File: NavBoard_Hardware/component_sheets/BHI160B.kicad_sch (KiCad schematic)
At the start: 12 parts, among them U2 BHI160B

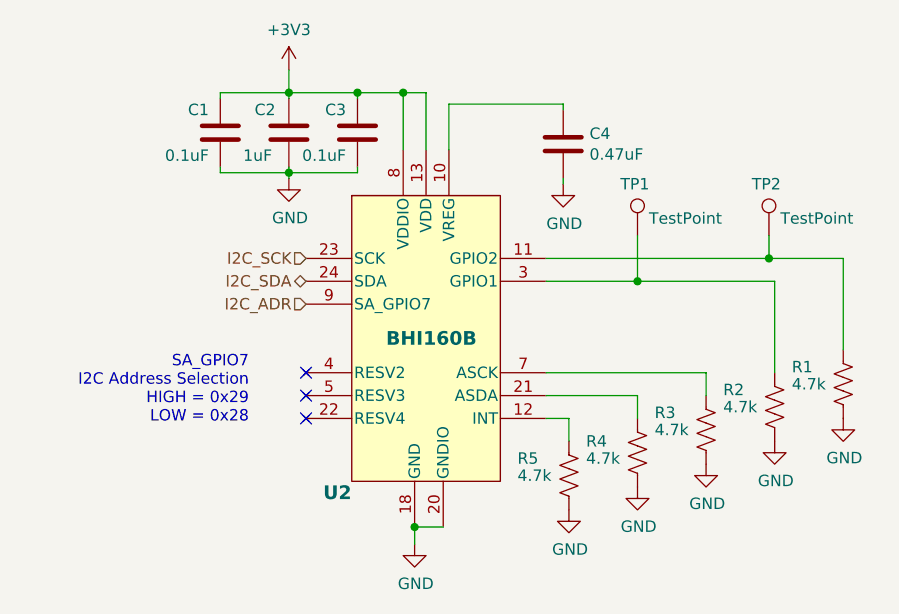
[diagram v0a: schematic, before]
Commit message: Most connections made on schematic
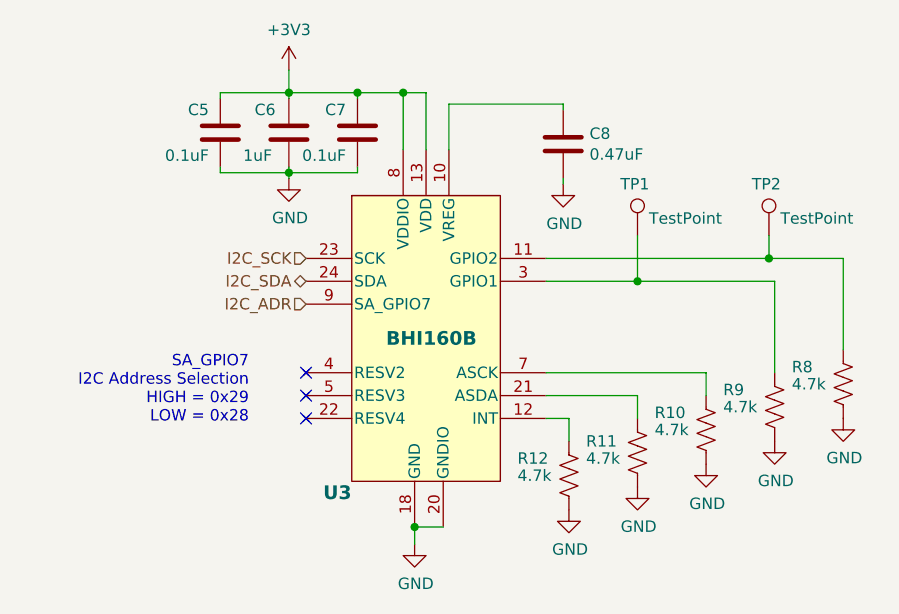
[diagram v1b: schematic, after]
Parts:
- renumbered C1 to C5, C2 to C6, C3 to C7, C4 to C8, R3 to R10, R4 to R11, R5 to R12, R1 to R8, R2 to R9, U2 to U3
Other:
- title: MRDT NavBoard - BHI160B -> MRDT NavBoard
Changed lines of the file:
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@@
   (paper "A4")
   (title_block
-    (title "MRDT NavBoard - BHI160B")
-    (date "2022-09-15")
-    (rev "1, 2023")
+    (title "MRDT NavBoard")
+    (date "2022-10-08")
+    (rev "3, 2023")
     (company "Thomas Francois, Missouri S&T Mars Rover Design Team")
-    (comment 1 "BHI160B Inertial Measurement Unit & Supporting Components")
-    (comment 2 "Provides Position and Acceleration Data")
+    (comment 1 "Teensy 4.1 Daughter Boards and Modules")
+    (comment 2 "and accelerometers")
+    (comment 3 "These boards are to be stacked together, and connects the Teensy to power, ethernet, ")
   )
   (junction (at 190.5 89.535) (diameter 0) (color 0 0 0 0)
@@
     (effects (font (size 1.27 1.27)) (justify right))
   )
-  (symbol (lib_id "Device:R_US") (at 191.135 106.045 0) (unit 1)
-    (in_bom yes) (on_board yes)
-    (property "Reference" "R2" (id 0) (at 185.42 104.14 0)
+  (symbol (lib_id "Device:R_US") (at 191.135 106.045 0)
+    (in_bom yes) (on_board yes)
+    (property "Reference" "R9" (id 0) (at 185.42 104.14 0)
       (effects (font (size 1.27 1.27)) (justify left))
     )
@@
     (pin "2")
   )
-  (symbol (lib_id "Device:R_US") (at 183.515 108.585 0) (unit 1)
-    (in_bom yes) (on_board yes)
-    (property "Reference" "R3" (id 0) (at 177.8 106.68 0)
+  (symbol (lib_id "Device:R_US") (at 183.515 108.585 0)
+    (in_bom yes) (on_board yes)
+    (property "Reference" "R10" (id 0) (at 177.8 106.68 0)
       (effects (font (size 1.27 1.27)) (justify left))
     )
@@
     (pin "2")
   )
-  (symbol (lib_id "power:GND") (at 151.13 121.285 0) (unit 1)
-    (in_bom yes) (on_board yes)
-    (property "Reference" "#PWR020" (id 0) (at 151.13 127.635 0)
+  (symbol (lib_id "power:GND") (at 151.13 121.285 0)
+    (in_bom yes) (on_board yes)
+    (property "Reference" "#PWR037" (id 0) (at 151.13 127.635 0)
       (effects (font (size 1.27 1.27)) hide)
     )
@@
     (pin "1")
   )
-  (symbol (lib_id "power:GND") (at 175.895 114.935 0) (unit 1)
-    (in_bom yes) (on_board yes)
-    (property "Reference" "#PWR018" (id 0) (at 175.895 121.285 0)
+  (symbol (lib_id "power:GND") (at 175.895 114.935 0)
+    (in_bom yes) (on_board yes)
+    (property "Reference" "#PWR035" (id 0) (at 175.895 121.285 0)
       (effects (font (size 1.27 1.27)) hide)
     )
@@
     (pin "1")
   )
-  (symbol (lib_id "Device:R_US") (at 198.755 103.505 0) (unit 1)
-    (in_bom yes) (on_board yes)
-    (property "Reference" "R1" (id 0) (at 193.04 101.6 0)
+  (symbol (lib_id "Device:R_US") (at 198.755 103.505 0)
+    (in_bom yes) (on_board yes)
+    (property "Reference" "R8" (id 0) (at 193.04 101.6 0)
       (effects (font (size 1.27 1.27)) (justify left))
     )
@@
     (pin "2")
   )
-  (symbol (lib_id "power:GND") (at 137.16 80.645 0) (unit 1)
-    (in_bom yes) (on_board yes)
-    (property "Reference" "#PWR013" (id 0) (at 137.16 86.995 0)
+  (symbol (lib_id "power:GND") (at 137.16 80.645 0)
+    (in_bom yes) (on_board yes)
+    (property "Reference" "#PWR030" (id 0) (at 137.16 86.995 0)
       (effects (font (size 1.27 1.27)) hide)
     )
@@
     (pin "1")
   )
-  (symbol (lib_id "power:GND") (at 167.64 81.28 0) (unit 1)
-    (in_bom yes) (on_board yes)
-    (property "Reference" "#PWR014" (id 0) (at 167.64 87.63 0)
+  (symbol (lib_id "power:GND") (at 167.64 81.28 0)
+    (in_bom yes) (on_board yes)
+    (property "Reference" "#PWR031" (id 0) (at 167.64 87.63 0)
       (effects (font (size 1.27 1.27)) hide)
     )
@@
     (pin "1")
   )
-  (symbol (lib_id "power:GND") (at 191.135 109.855 0) (unit 1)
-    (in_bom yes) (on_board yes)
-    (property "Reference" "#PWR016" (id 0) (at 191.135 116.205 0)
+  (symbol (lib_id "power:GND") (at 191.135 109.855 0)
+    (in_bom yes) (on_board yes)
+    (property "Reference" "#PWR033" (id 0) (at 191.135 116.205 0)
       (effects (font (size 1.27 1.27)) hide)
     )
@@
     (pin "1")
   )
-  (symbol (lib_id "Device:C") (at 167.64 76.835 0) (unit 1)
-    (in_bom yes) (on_board yes)
-    (property "Reference" "C4" (id 0) (at 170.561 75.6666 0)
+  (symbol (lib_id "Device:C") (at 167.64 76.835 0)
+    (in_bom yes) (on_board yes)
+    (property "Reference" "C8" (id 0) (at 170.561 75.6666 0)
       (effects (font (size 1.27 1.27)) (justify left))
     )
@@
     (pin "2")
   )
-  (symbol (lib_id "MRDT_Sensors:BHI160B") (at 152.4 97.155 0) (unit 1)
-    (in_bom yes) (on_board yes)
-    (property "Reference" "U2" (id 0) (at 140.97 115.57 0)
+  (symbol (lib_id "MRDT_Sensors:BHI160B") (at 152.4 97.155 0)
+    (in_bom yes) (on_board yes)
+    (property "Reference" "U3" (id 0) (at 140.97 115.57 0)
       (effects (font (size 1.524 1.524) bold) (justify left))
     )
@@
     (pin "9")
   )
-  (symbol (lib_id "Device:R_US") (at 168.275 113.665 0) (unit 1)
-    (in_bom yes) (on_board yes)
-    (property "Reference" "R5" (id 0) (at 162.56 111.76 0)
+  (symbol (lib_id "Device:R_US") (at 168.275 113.665 0)
+    (in_bom yes) (on_board yes)
+    (property "Reference" "R12" (id 0) (at 162.56 111.76 0)
       (effects (font (size 1.27 1.27)) (justify left))
     )
@@
     (pin "2")
   )
-  (symbol (lib_id "power:+3V3") (at 137.16 68.58 0) (unit 1)
-    (in_bom yes) (on_board yes)
-    (property "Reference" "#PWR012" (id 0) (at 137.16 72.39 0)
+  (symbol (lib_id "power:+3V3") (at 137.16 68.58 0)
+    (in_bom yes) (on_board yes)
+    (property "Reference" "#PWR029" (id 0) (at 137.16 72.39 0)
       (effects (font (size 1.27 1.27)) hide)
     )
@@
     (pin "1")
   )
-  (symbol (lib_id "Connector:TestPoint") (at 190.5 86.995 0) (unit 1)
+  (symbol (lib_id "Connector:TestPoint") (at 190.5 86.995 0)
     (in_bom yes) (on_board yes)
     (property "Reference" "TP2" (id 0) (at 188.595 81.28 0)
@@
     (pin "1")
   )
-  (symbol (lib_id "power:GND") (at 198.755 107.315 0) (unit 1)
-    (in_bom yes) (on_board yes)
-    (property "Reference" "#PWR015" (id 0) (at 198.755 113.665 0)
+  (symbol (lib_id "power:GND") (at 198.755 107.315 0)
+    (in_bom yes) (on_board yes)
+    (property "Reference" "#PWR032" (id 0) (at 198.755 113.665 0)
       (effects (font (size 1.27 1.27)) hide)
     )
@@
     (pin "1")
   )
-  (symbol (lib_id "Device:C") (at 144.78 75.565 0) (mirror y) (unit 1)
-    (in_bom yes) (on_board yes)
-    (property "Reference" "C3" (id 0) (at 143.51 73.025 0)
+  (symbol (lib_id "Device:C") (at 144.78 75.565 0) (mirror y)
+    (in_bom yes) (on_board yes)
+    (property "Reference" "C7" (id 0) (at 143.51 73.025 0)
       (effects (font (size 1.27 1.27)) (justify left))
     )
@@
     (pin "2")
   )
-  (symbol (lib_id "power:GND") (at 183.515 112.395 0) (unit 1)
-    (in_bom yes) (on_board yes)
-    (property "Reference" "#PWR017" (id 0) (at 183.515 118.745 0)
+  (symbol (lib_id "power:GND") (at 183.515 112.395 0)
+    (in_bom yes) (on_board yes)
+    (property "Reference" "#PWR034" (id 0) (at 183.515 118.745 0)
       (effects (font (size 1.27 1.27)) hide)
     )
@@
     (pin "1")
   )
-  (symbol (lib_id "Device:C") (at 129.54 75.565 0) (mirror y) (unit 1)
-    (in_bom yes) (on_board yes)
-    (property "Reference" "C1" (id 0) (at 128.27 73.025 0)
+  (symbol (lib_id "Device:C") (at 129.54 75.565 0) (mirror y)
+    (in_bom yes) (on_board yes)
+    (property "Reference" "C5" (id 0) (at 128.27 73.025 0)
       (effects (font (size 1.27 1.27)) (justify left))
     )
@@
     (pin "2")
   )
-  (symbol (lib_id "Device:R_US") (at 175.895 111.125 0) (unit 1)
-    (in_bom yes) (on_board yes)
-    (property "Reference" "R4" (id 0) (at 170.18 109.855 0)
+  (symbol (lib_id "Device:R_US") (at 175.895 111.125 0)
+    (in_bom yes) (on_board yes)
+    (property "Reference" "R11" (id 0) (at 170.18 109.855 0)
       (effects (font (size 1.27 1.27)) (justify left))
     )
@@
     (pin "2")
   )
-  (symbol (lib_id "Device:C") (at 137.16 75.565 0) (unit 1)
-    (in_bom yes) (on_board yes)
-    (property "Reference" "C2" (id 0) (at 133.35 73.025 0)
+  (symbol (lib_id "Device:C") (at 137.16 75.565 0)
+    (in_bom yes) (on_board yes)
+    (property "Reference" "C6" (id 0) (at 133.35 73.025 0)
       (effects (font (size 1.27 1.27)) (justify left))
     )
@@
     (pin "2")
   )
-  (symbol (lib_id "power:GND") (at 168.275 117.475 0) (unit 1)
-    (in_bom yes) (on_board yes)
-    (property "Reference" "#PWR019" (id 0) (at 168.275 123.825 0)
+  (symbol (lib_id "power:GND") (at 168.275 117.475 0)
+    (in_bom yes) (on_board yes)
+    (property "Reference" "#PWR036" (id 0) (at 168.275 123.825 0)
       (effects (font (size 1.27 1.27)) hide)
     )
@@
     (pin "1")
   )
-  (symbol (lib_id "Connector:TestPoint") (at 175.895 86.995 0) (unit 1)
+  (symbol (lib_id "Connector:TestPoint") (at 175.895 86.995 0)
     (in_bom yes) (on_board yes)
     (property "Reference" "TP1" (id 0) (at 173.99 81.28 0)
